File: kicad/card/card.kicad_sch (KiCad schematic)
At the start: 34 parts, among them SW1 USB_BOOT, SW2 RESET, U1 RP2350A, U2 TLV70030_SOT23-5, U3 W25Q128, Y1 12MHz

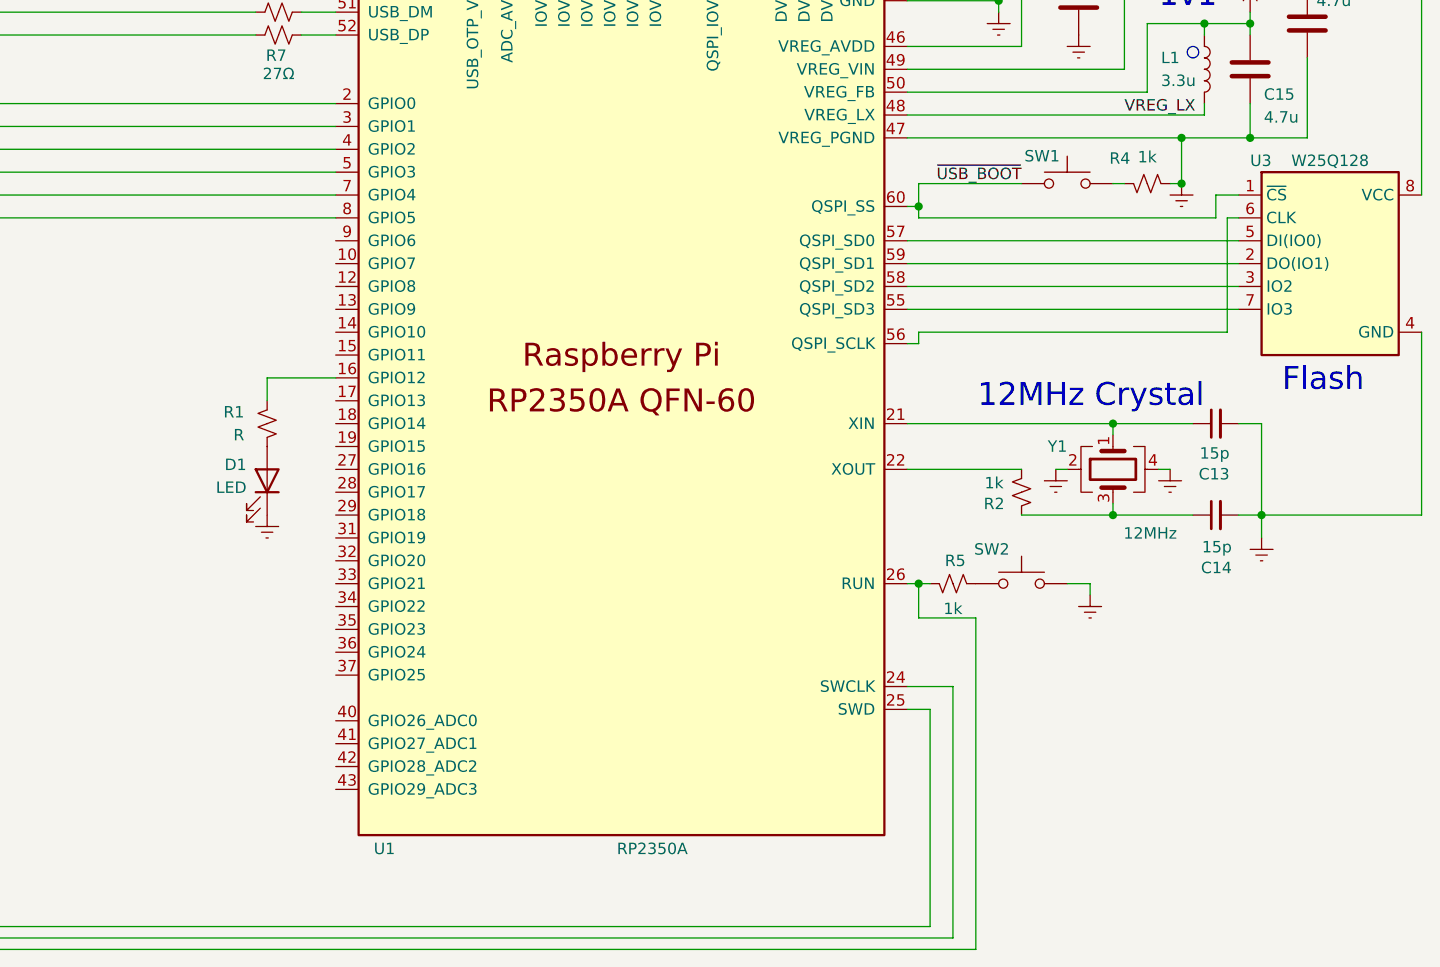
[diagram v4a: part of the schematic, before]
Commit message: added 2mm headers and fabrication files
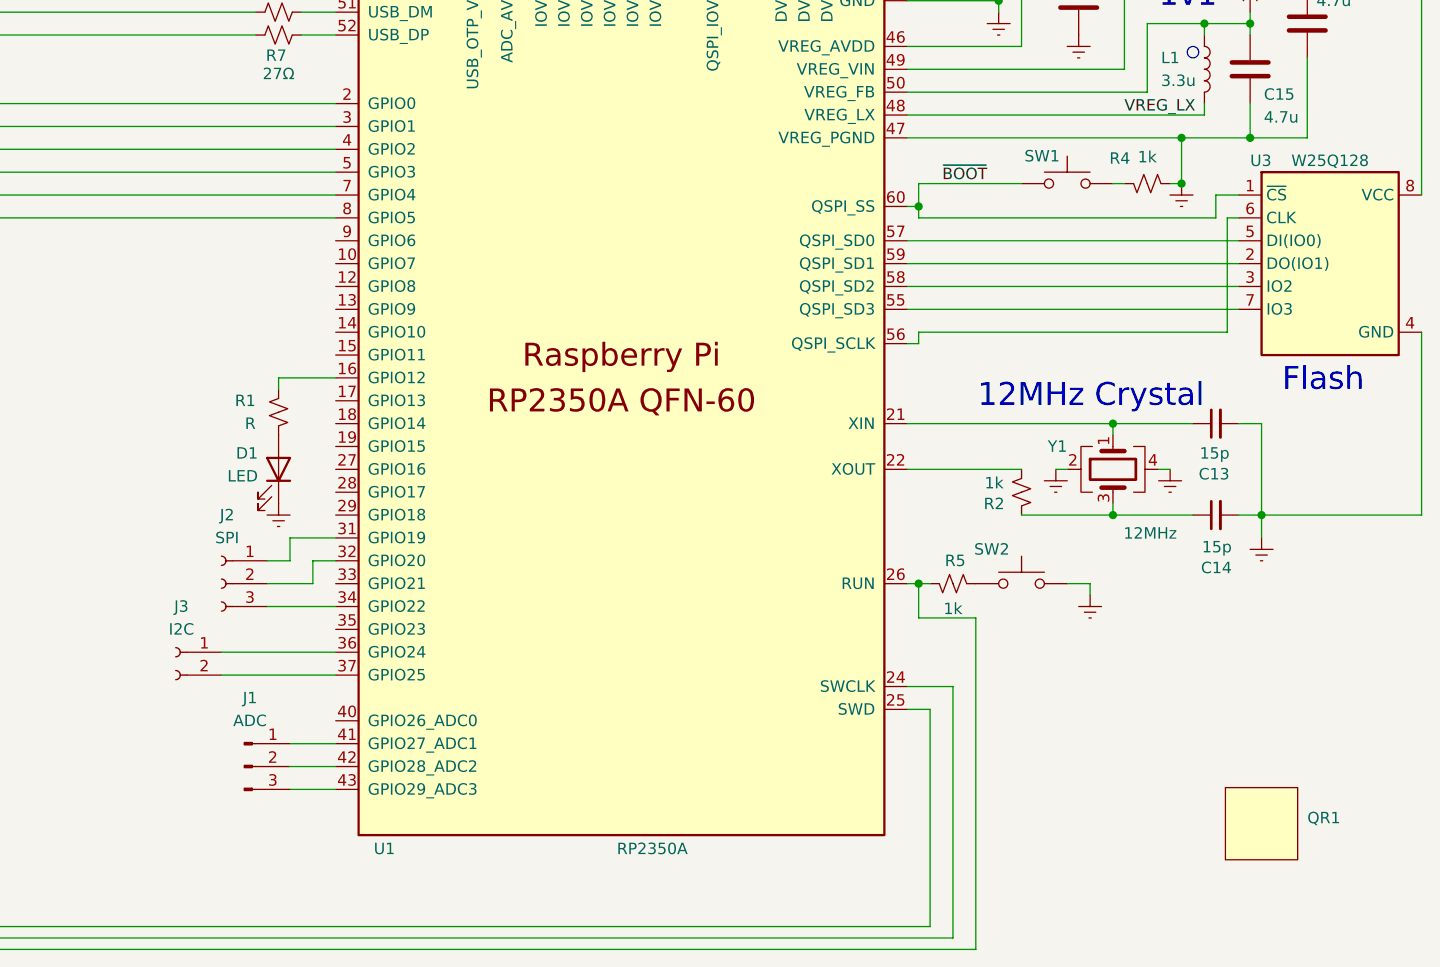
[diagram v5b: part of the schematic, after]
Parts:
- added J1: ADC, Connector_PinHeader_2.00mm:PinHeader_1x03_P2.00mm_Vertical, symbol Connector:Conn_01x03_Pin
- added J2: SPI, Connector_PinHeader_2.00mm:PinHeader_1x03_P2.00mm_Vertical, symbol Connector:Conn_01x03_Socket
- added J3: I2C, Connector_PinHeader_2.00mm:PinHeader_1x02_P2.00mm_Vertical, symbol Connector:Conn_01x02_Socket
- added QR1: ~, DEFAULT:QR_8x8, symbol DEFAULT:QR_8x8
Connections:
- net at U1.31 (GPIO19): now also J2.1 (Pin_1)
- net at U1.32 (GPIO20): now also J2.2 (Pin_2)
- net at U1.34 (GPIO22): now also J2.3 (Pin_3)
- net at U1.36 (GPIO24): now also J3.1 (Pin_1)
- net at U1.37 (GPIO25): now also J3.2 (Pin_2)
- net at U1.41 (GPIO27_ADC1): now also J1.1 (Pin_1)
- net at U1.42 (GPIO28_ADC2): now also J1.2 (Pin_2)
- net at U1.43 (GPIO29_ADC3): now also J1.3 (Pin_3)
- net ~{USB_BOOT} renamed ~{BOOT}
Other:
- moved on the sheet: D1, R1

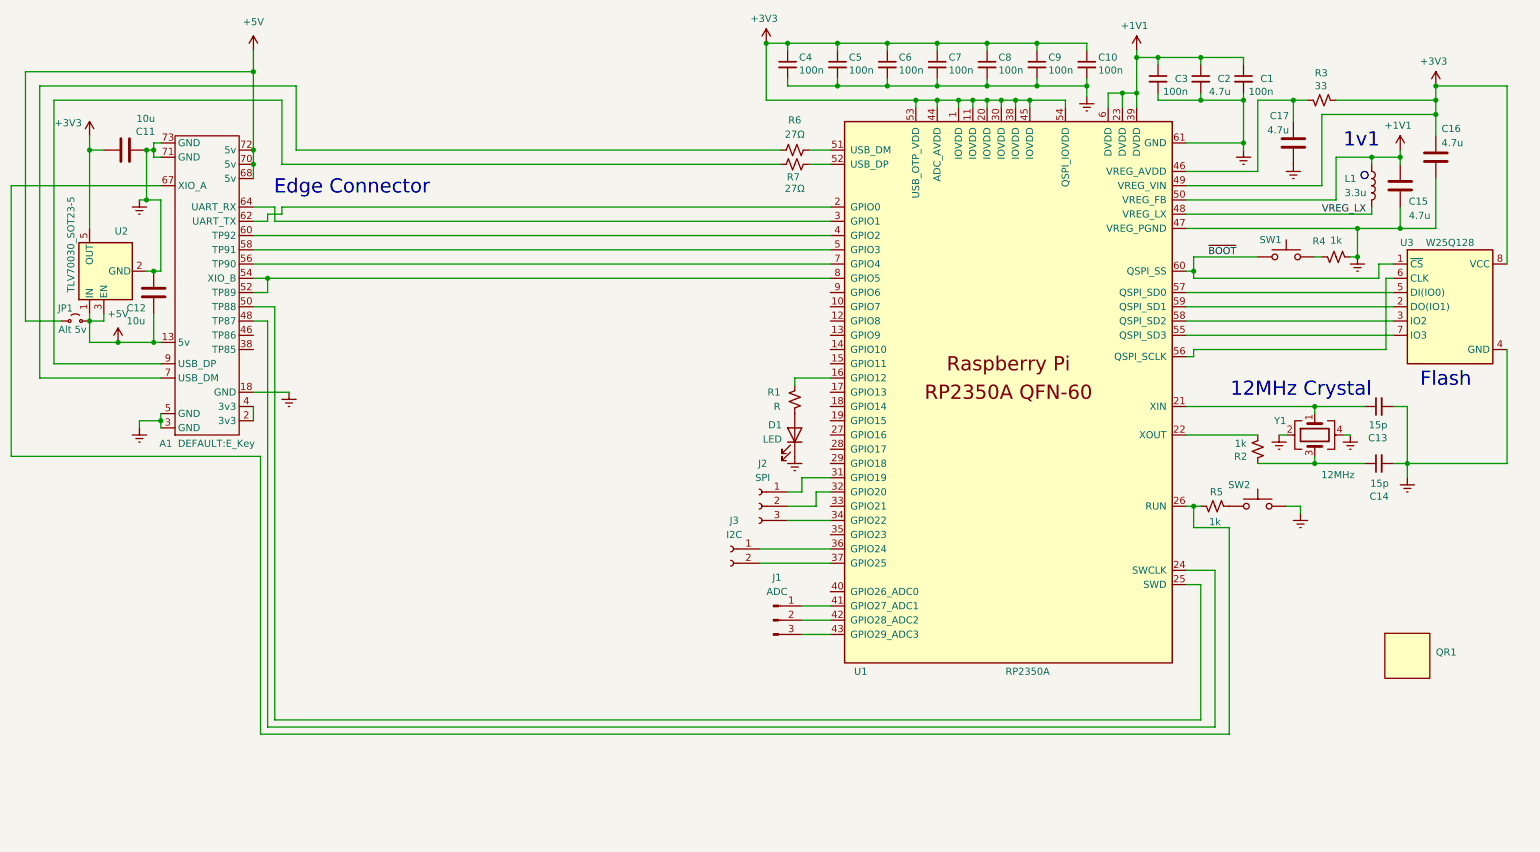
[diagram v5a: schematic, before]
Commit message: BNO08x IMU
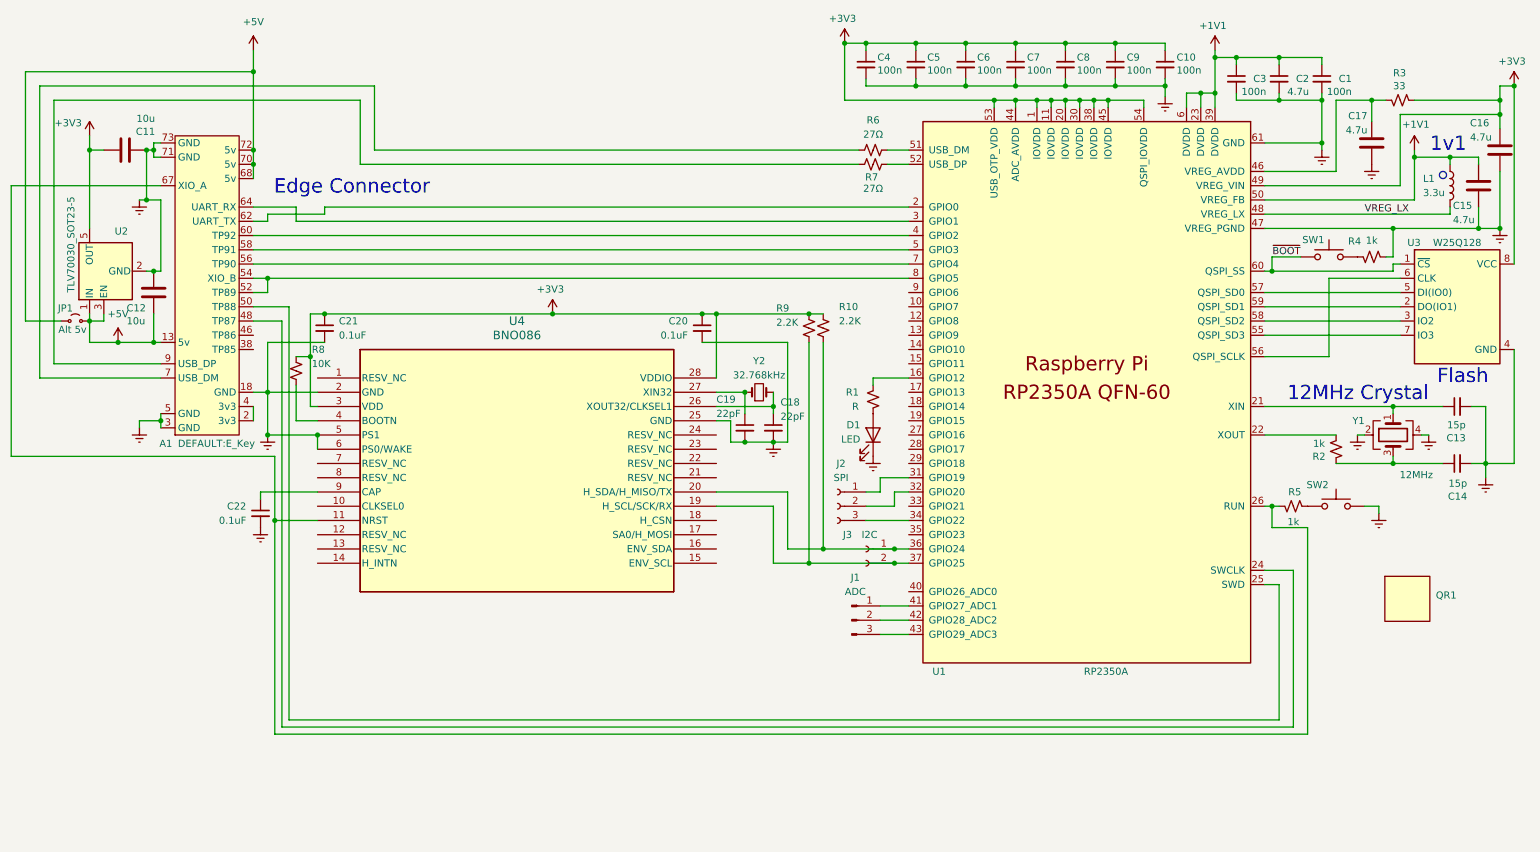
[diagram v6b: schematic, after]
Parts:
- added C18, C19: 22pF, Capacitor_SMD:C_0402_1005Metric, symbol Device:C_Small
- added C20, C21, C22: 0.1uF, Capacitor_SMD:C_0402_1005Metric, symbol Device:C_Small
- added R10, R9: 2.2K, Resistor_SMD:R_0402_1005Metric, symbol Device:R_Small_US
- added R8: 10K, Resistor_SMD:R_0402_1005Metric, symbol Device:R_Small_US
- added U4: BNO086, QFN28_BNO086_CEV, symbol DEFAULT:BNO086
- added Y2: 32.768kHz, Crystal:Crystal_SMD_2012-2Pin_2.0x1.2mm, symbol Device:Crystal_Small
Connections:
- net +3V3: now also C20.1, C21.1, R10.1, R8.1, R9.1, U4.28 (VDDIO), U4.3 (VDD)
- net GND: now also C18.2, C19.2, C20.2, C21.2, C22.2, U4.2 (GND), U4.25 (GND), U4.5 (PS1), U4.6 (PS0/WAKE)
- net at J3.1 (Pin_1), U1.36 (GPIO24): now also R10.2, U4.20 (H_SDA/H_MISO/TX)
- net at J3.2 (Pin_2), U1.37 (GPIO25): now also R9.2, U4.19 (H_SCL/SCK/RX)
- net at A1.67 (XIO_A), R5.1, U1.26 (RUN): now also U4.11 (NRST)
- new net: C18.1, U4.26 (XOUT32/CLKSEL1), Y2.2
- new net: C19.1, U4.27 (XIN32), Y2.1
- new net: R8.2, U4.4 (BOOTN)
- new net: C22.1, U4.9 (CAP)
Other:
- title: minimal blink layout -> M.2 Card - minimal blink & IMU layout
- moved on the sheet: C1, C10, C13, C14, C15, C16, C17, C2, C3, C4, C5, C6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

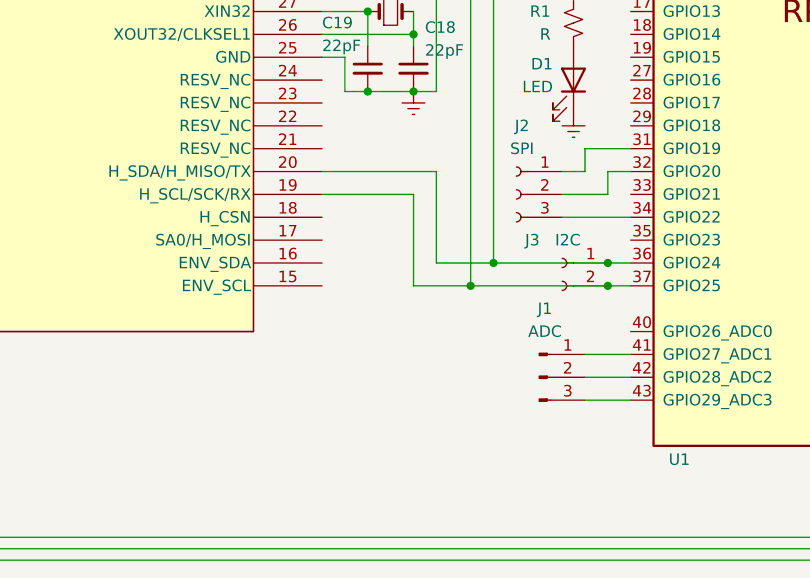
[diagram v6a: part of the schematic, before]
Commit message: 0.1" Breadboard header
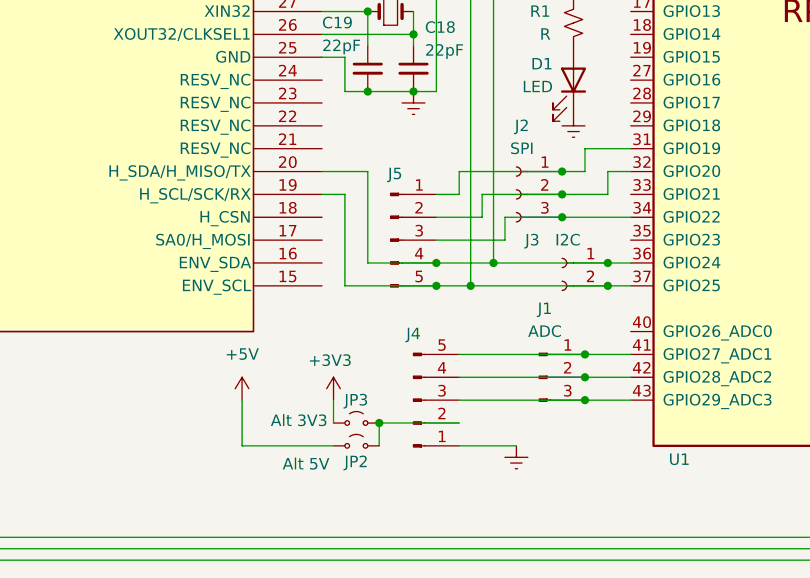
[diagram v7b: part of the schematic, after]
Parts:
- added J4, J5: Conn_01x05_Pin, Connector_PinHeader_2.54mm:PinHeader_1x05_P2.54mm_Horizontal, symbol Connector:Conn_01x05_Pin
- added JP2: Alt 5V, Jumper:SolderJumper-2_P1.3mm_Open_TrianglePad1.0x1.5mm, symbol Jumper:Jumper_2_Small_Open
- added JP3: Alt 3V3, Jumper:SolderJumper-2_P1.3mm_Open_TrianglePad1.0x1.5mm, symbol Jumper:Jumper_2_Small_Open
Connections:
- net +3V3: now also JP3.1 (A)
- net +5V: now also JP2.1 (A)
- net GND: now also J4.1 (Pin_1)
- net at J3.1 (Pin_1), R10.2, U1.36 (GPIO24)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: now also J5.4 (Pin_4)
- net at J3.2 (Pin_2), R9.2, U1.37 (GPIO25)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: now also J5.5 (Pin_5)
- net at J2.1 (Pin_1), U1.31 (GPIO19): now also J5.1 (Pin_1)
- net at J2.2 (Pin_2), U1.32 (GPIO20): now also J5.2 (Pin_2)
- net at J2.3 (Pin_3), U1.34 (GPIO22): now also J5.3 (Pin_3)
- net at J1.1 (Pin_1), U1.41 (GPIO27_ADC1): now also J4.5 (Pin_5)
- net at J1.2 (Pin_2), U1.42 (GPIO28_ADC2): now also J4.4 (Pin_4)
- net at J1.3 (Pin_3), U1.43 (GPIO29_ADC3): now also J4.3 (Pin_3)
- new net: J4.2 (Pin_2), JP2.2 (B), JP3.2 (B)
